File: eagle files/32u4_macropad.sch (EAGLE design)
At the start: 91 parts, among them J1 TYPE-C-31-M-12, Q1 16MHz, SW2 SWITCH-SMD-EVP-BB2A9B00

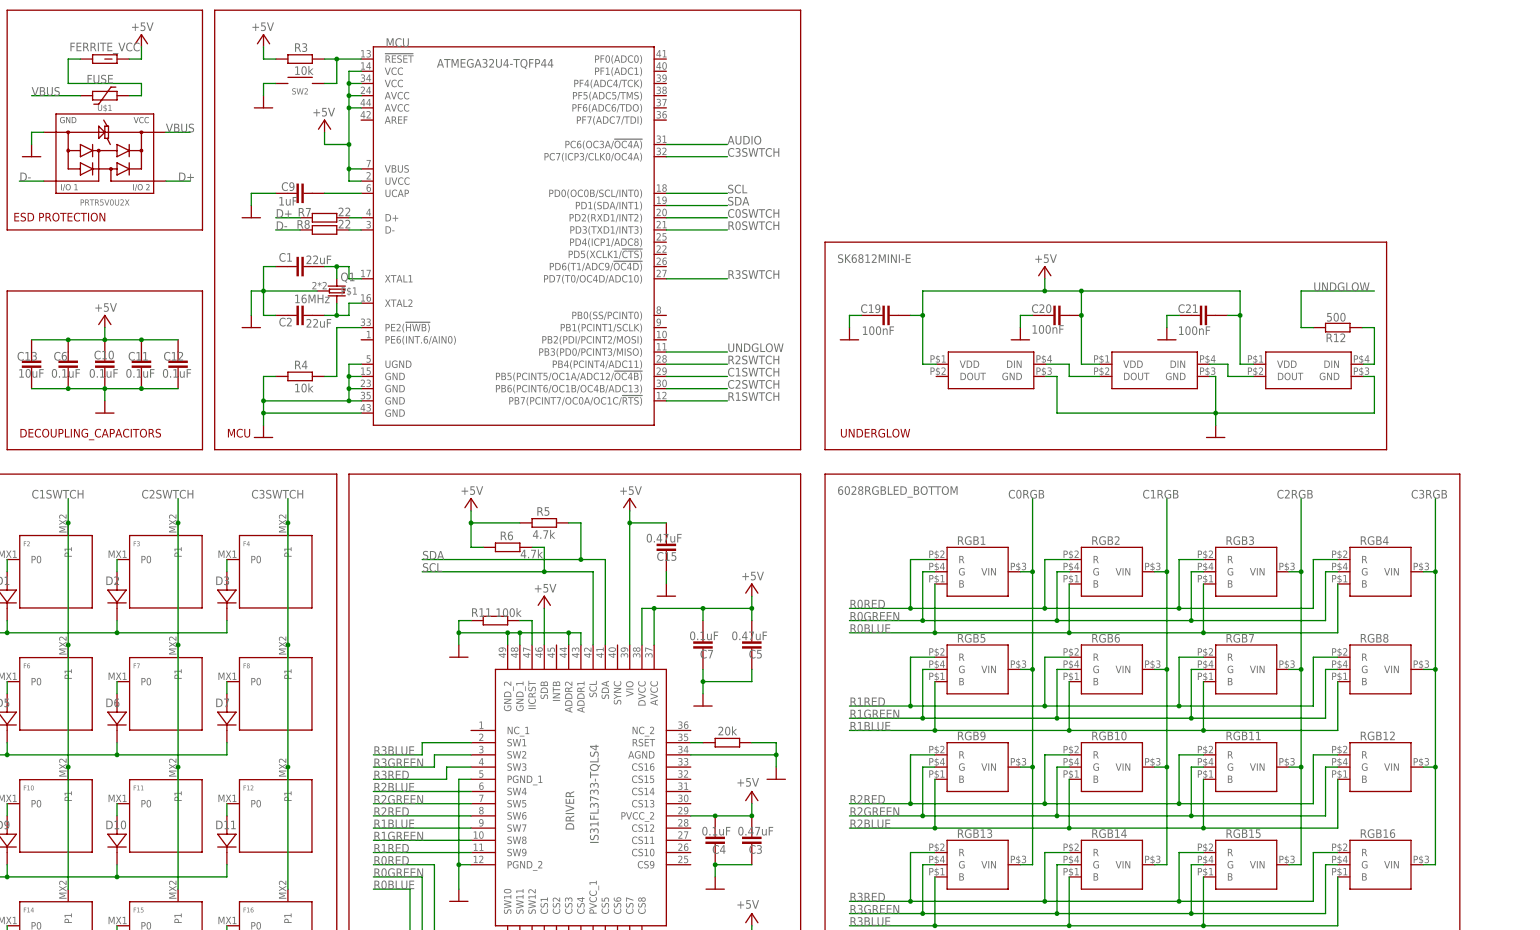
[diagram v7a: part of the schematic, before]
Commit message: Small routing fixes, added credits in sch and brd
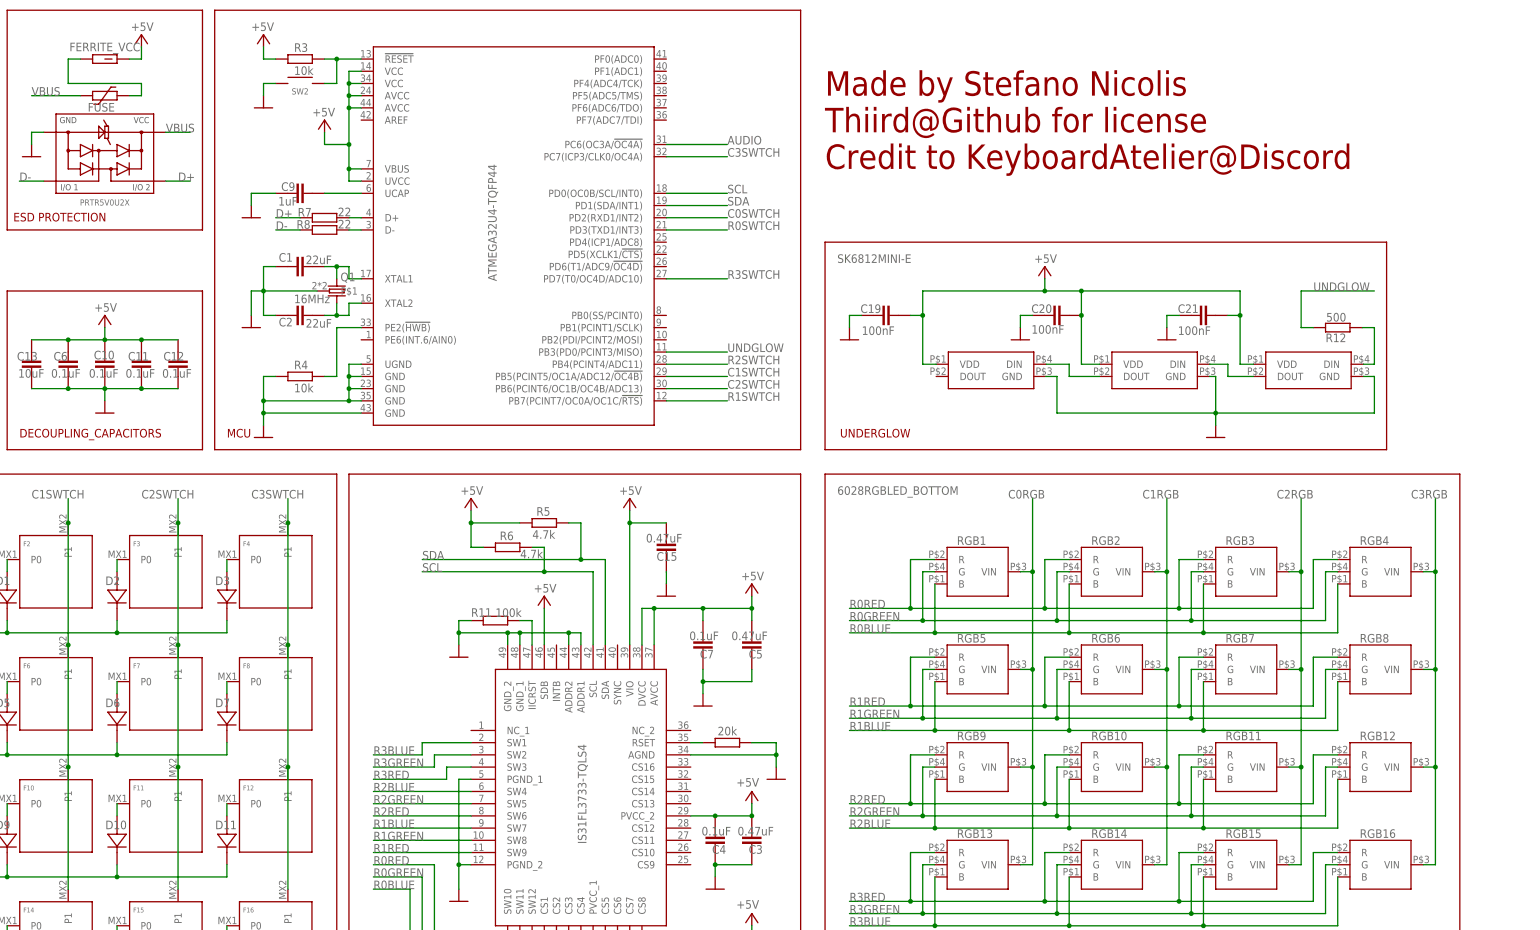
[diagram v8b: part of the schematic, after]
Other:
- note added: "Credit to KeyboardAtelier@Discord"
- note added: "Made by Stefano Nicolis Thiird@Github for license"
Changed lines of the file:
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@@
 <text x="-205.74" y="4.572" size="1.778" layer="94">SMD_BUZZER</text>
 <text x="-215.9" y="58.42" size="1.778" layer="94">USB-C PORT</text>
+<text x="2.54" y="68.58" size="5.08" layer="94">Made by Stefano Nicolis
+Thiird@Github for license</text>
+<text x="2.54" y="60.96" size="5.08" layer="94">Credit to KeyboardAtelier@Discord</text>
 </plain>
 <instances>
@@
 </instance>
 <instance part="MCU" gate="G$1" x="-60.96" y="48.26" smashed="yes">
-<attribute name="NAME" x="-88.9" y="86.36" size="1.778" layer="95"/>
-<attribute name="VALUE" x="-78.232" y="82.042" size="1.778" layer="96"/>
+<attribute name="VALUE" x="-65.786" y="37.592" size="1.778" layer="96" rot="R90"/>
 </instance>
 <instance part="R7" gate="G$1" x="-101.6" y="50.8" smashed="yes">
@@
 </instance>
 <instance part="DRIVER" gate="G$1" x="-71.12" y="-55.88" smashed="yes">
-<attribute name="NAME" x="-50.546" y="-76.708" size="1.778" layer="95" rot="R90" align="center-left"/>
-<attribute name="VALUE" x="-45.466" y="-79.502" size="1.778" layer="96" rot="MR90" align="center-left"/>
+<attribute name="VALUE" x="-48.006" y="-79.502" size="1.778" layer="96" rot="MR90" align="center-left"/>
 </instance>
 <instance part="P+3" gate="VCC" x="-71.12" y="-7.62" smashed="yes">
@@
 </instance>
 <instance part="U$1" gate="G$1" x="-147.32" y="63.5" smashed="yes">
-<attribute name="NAME" x="-147.32" y="73.66" size="1.27" layer="95" font="vector" align="center"/>
 <attribute name="VALUE" x="-147.32" y="53.975" size="1.27" layer="95" font="vector" align="center"/>
 </instance>
@@
 </instance>
 <instance part="FUSE" gate="G$1" x="-147.32" y="76.2" smashed="yes">
-<attribute name="NAME" x="-151.13" y="78.74" size="1.778" layer="95"/>
+<attribute name="NAME" x="-150.876" y="72.898" size="1.778" layer="95"/>
 </instance>
 <instance part="FERRITE_USB" gate="G$1" x="-182.88" y="66.04" smashed="yes">
@@
 </drawing>
 <compatibility>
+<note version="6.3" minversion="6.2.2" severity="warning">
+Since Version 6.2.2 text objects can contain more than one line,
+which will not be processed correctly with this version.
+</note>
 <note version="8.2" severity="warning">
 Since Version 8.2, EAGLE supports online libraries. The ids
